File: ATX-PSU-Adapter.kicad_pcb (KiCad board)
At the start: 2 copper layers, 65 x 45 mm, 33 parts, among them J1 ATX-24, J10 Conn_01x01, J11 Conn_01x01, J12 Conn_01x01, J13 Conn_01x01, J14 Conn_01x01, J15 Conn_01x01, J16 Conn_01x01, J17 Conn_01x01, J18 Conn_01x01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

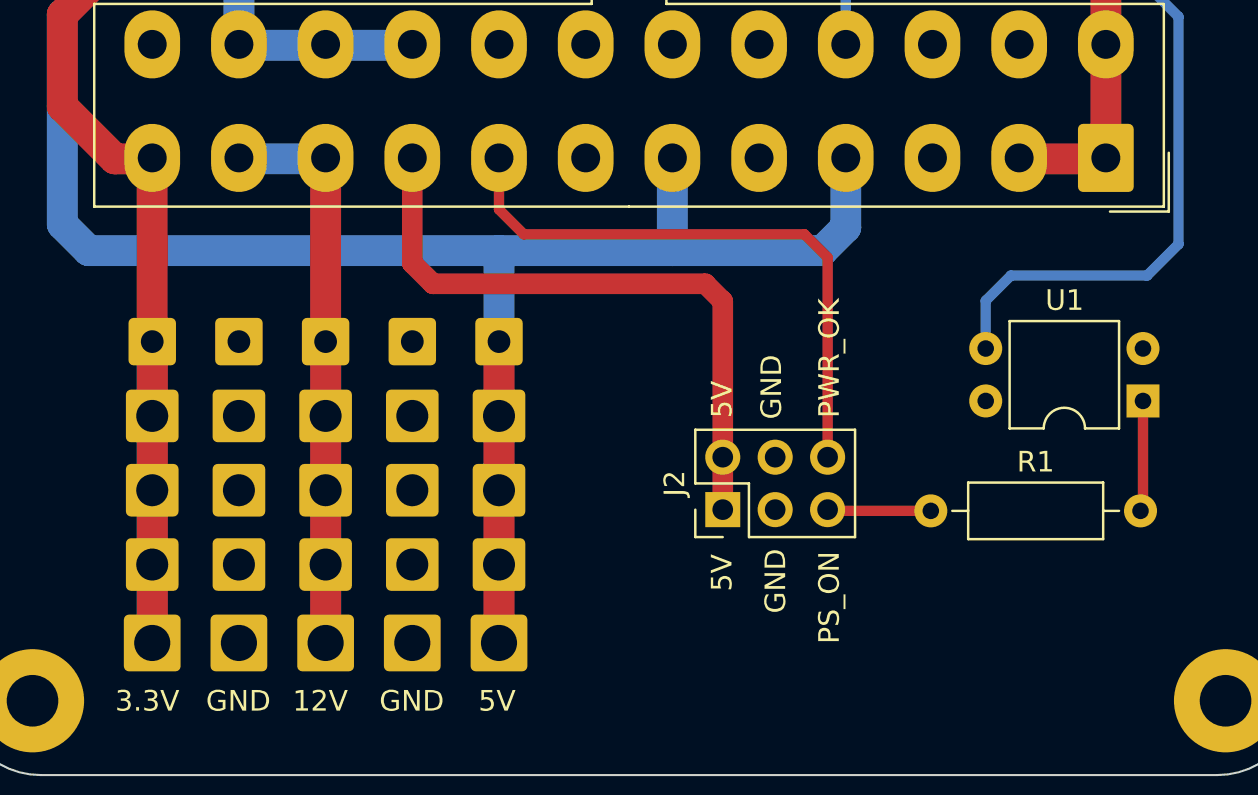
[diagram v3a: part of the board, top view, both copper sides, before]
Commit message: Switch 5VSB and GND
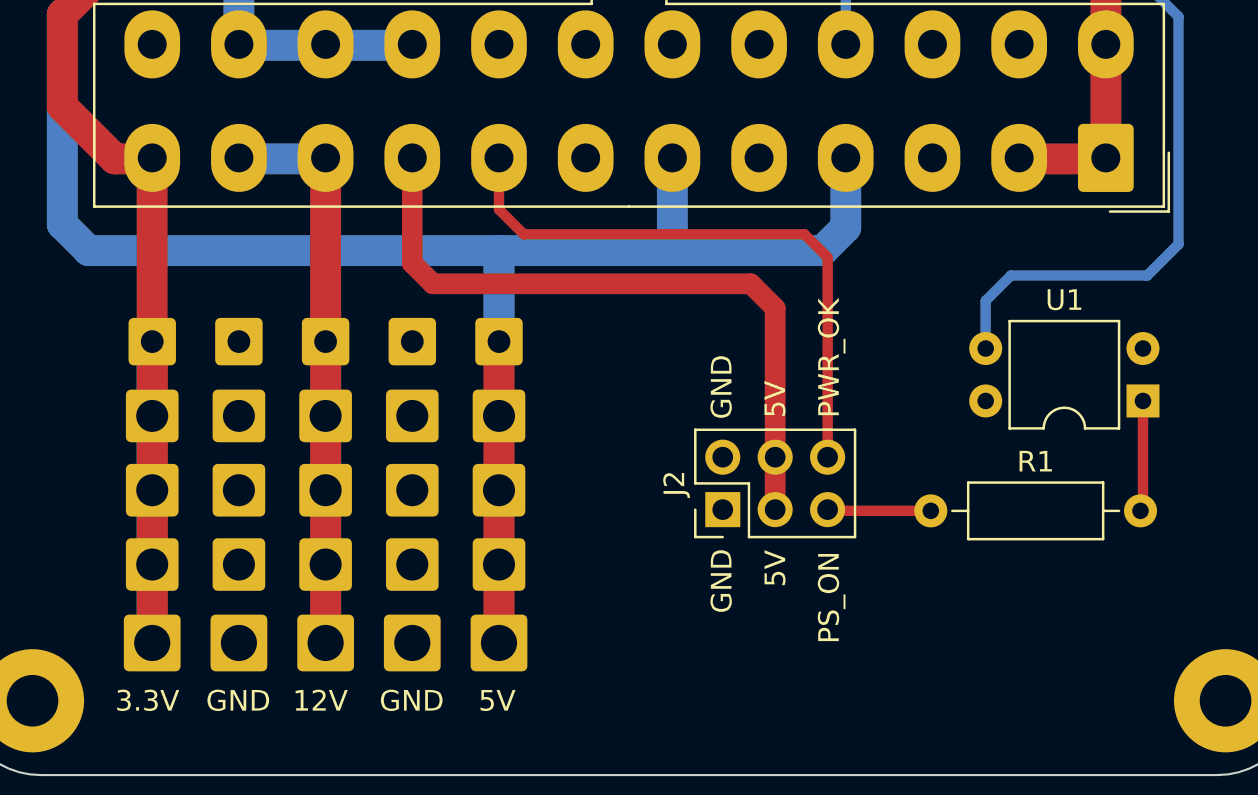
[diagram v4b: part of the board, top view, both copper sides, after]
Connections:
- J2 pad 1: /5VSB -> GND
- J2 pad 2: /5VSB -> GND
- J2 pad 3: GND -> /5VSB
- J2 pad 4: GND -> /5VSB
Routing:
- net /5VSB: track 31.0 -> 33.3 mm

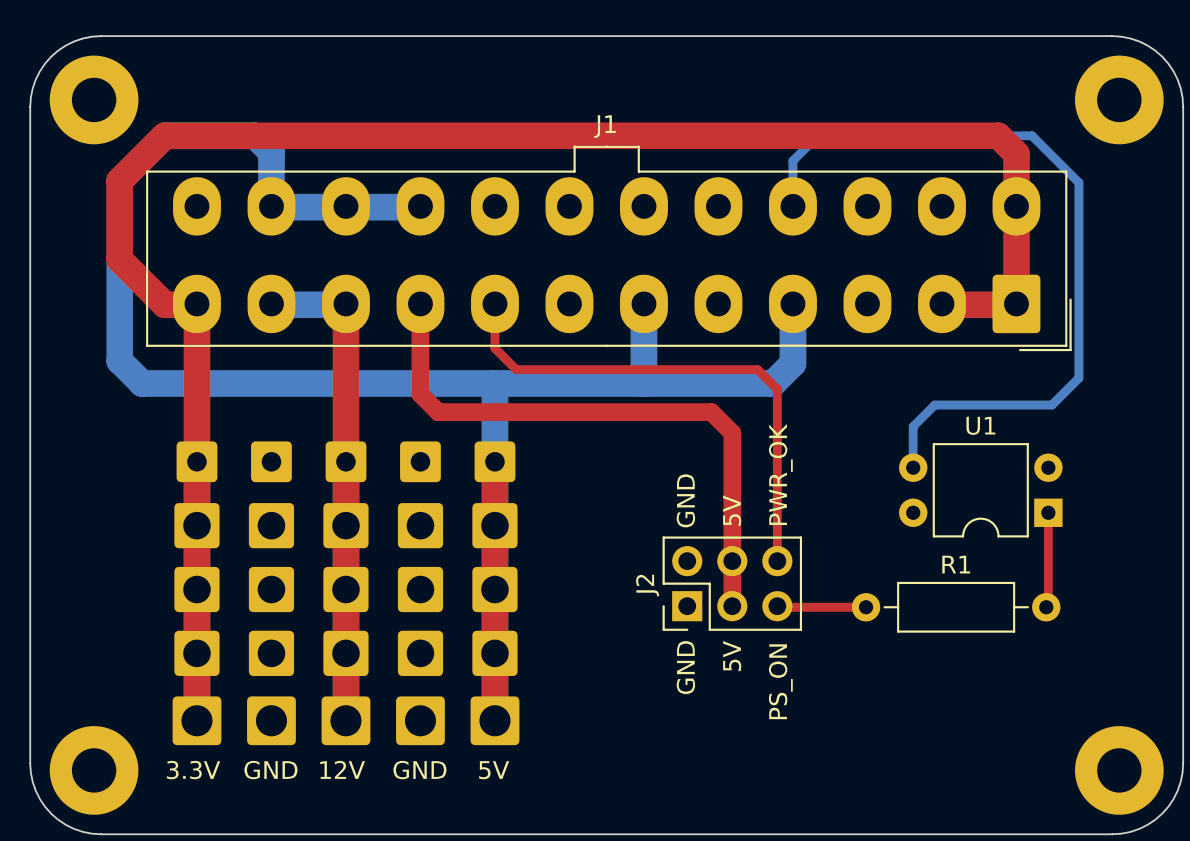
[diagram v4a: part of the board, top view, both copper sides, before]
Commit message: Fix: ATX Connector Footprint, Optocoupler wiring
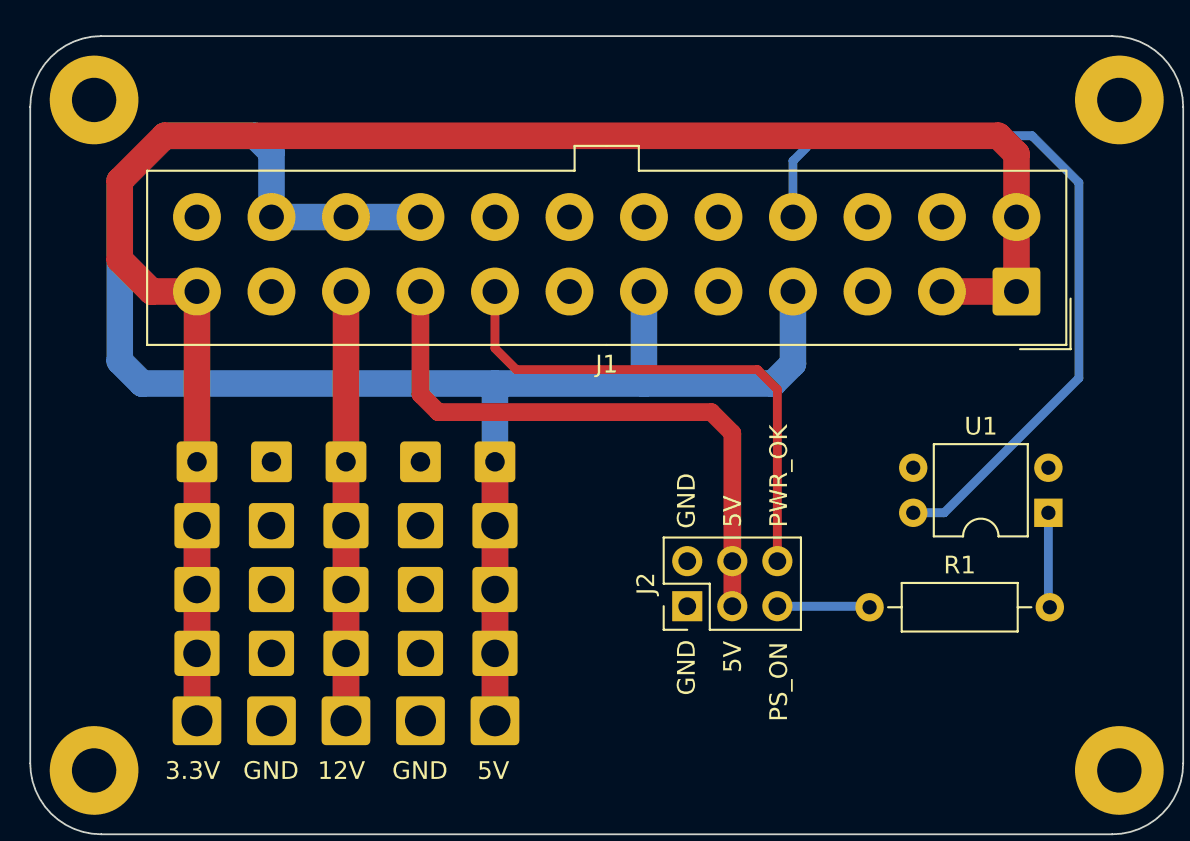
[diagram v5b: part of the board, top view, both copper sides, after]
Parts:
- J1: footprint Connector_Molex:Molex_Mini-Fit_Jr_5566-24A_2x12_P4.20mm_Vertical -> Connector_Molex_Mod:Molex_Mod_Mini-Fit_Jr_5566-24A_2x12_P4.20mm_Vertical
- moved J1 0.70 mm to (80.6, 39.4)
- moved R1 0.20 mm to (72.3, 57.2)
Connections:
- J1 pad 16: /PS_ON -> Net-(J1-PS_ON#)
- U1 pad 3: /PS_ON -> GND
- U1 pad 4: GND -> Net-(J1-PS_ON#)
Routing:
- net Net-(J1-PS_ON#): track 0.00 -> 44.5 mm
- net /PS_ON: track 44.2 -> 0.00 mm
- net /12V: track 42.3 -> 38.8 mm
- net /5V: track 112.1 -> 114.1 mm
- net /PWR_OK: track 29.0 -> 29.8 mm
- net /5VSB: track 33.3 -> 34.0 mm

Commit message: Replace ATX connector, wiring and layout
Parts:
- J1: footprint Connector_Molex_Mod:Molex_Mod_Mini-Fit_Jr_5566-24A_2x12_P4.20mm_Vertical -> Connector_Molex:Molex_Mini-Fit_Jr_5566-24A_2x12_P4.20mm_Vertical
- moved J7 51.6 mm to (83.1, 46.6), turned to 180 degrees
- moved J3 50.2 mm to (83.1, 61.2), turned to 180 degrees
- moved J6 49.6 mm to (83.1, 50.4), turned to 180 degrees
- moved J4 49.0 mm to (83.1, 57.6), turned to 180 degrees
- moved J5 48.7 mm to (83.1, 54.0), turned to 180 degrees
- moved J1 44.2 mm to (36.9, 32.9), turned to 0 degrees
- moved J12 43.7 mm to (78.9, 46.6), turned to 180 degrees
- moved J8 42.1 mm to (78.9, 61.2), turned to 180 degrees
- moved J11 41.4 mm to (78.9, 50.4), turned to 180 degrees
- moved J9 40.6 mm to (78.9, 57.6), turned to 180 degrees
- moved J10 40.4 mm to (78.9, 54.0), turned to 180 degrees
- moved J17 36.1 mm to (74.7, 46.6), turned to 180 degrees
- moved J13 34.2 mm to (74.7, 61.2), turned to 180 degrees
- moved J16 33.3 mm to (74.7, 50.4), turned to 180 degrees
- moved J14 32.3 mm to (74.7, 57.6), turned to 180 degrees
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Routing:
- net /5VSB: track 34.0 -> 78.8 mm, vias 0 -> 1
- net /PWR_OK: track 29.8 -> 72.0 mm
- net /12V: track 38.8 -> 73.6 mm
- net Net-(J1-PS_ON#): track 44.5 -> 13.2 mm
- net GND: track 0.00 -> 29.2 mm
- net /5V: track 114.1 -> 129.9 mm
- net Net-(J2-Pin_5): track 5.31 -> 8.20 mm
- net /3.3V: track 112.3 -> 113.6 mm
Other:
- board size 65 x 45 mm -> 66 x 48 mm
